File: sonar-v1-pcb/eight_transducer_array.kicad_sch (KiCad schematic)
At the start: 22 parts, among them U201 ADS8568SPM

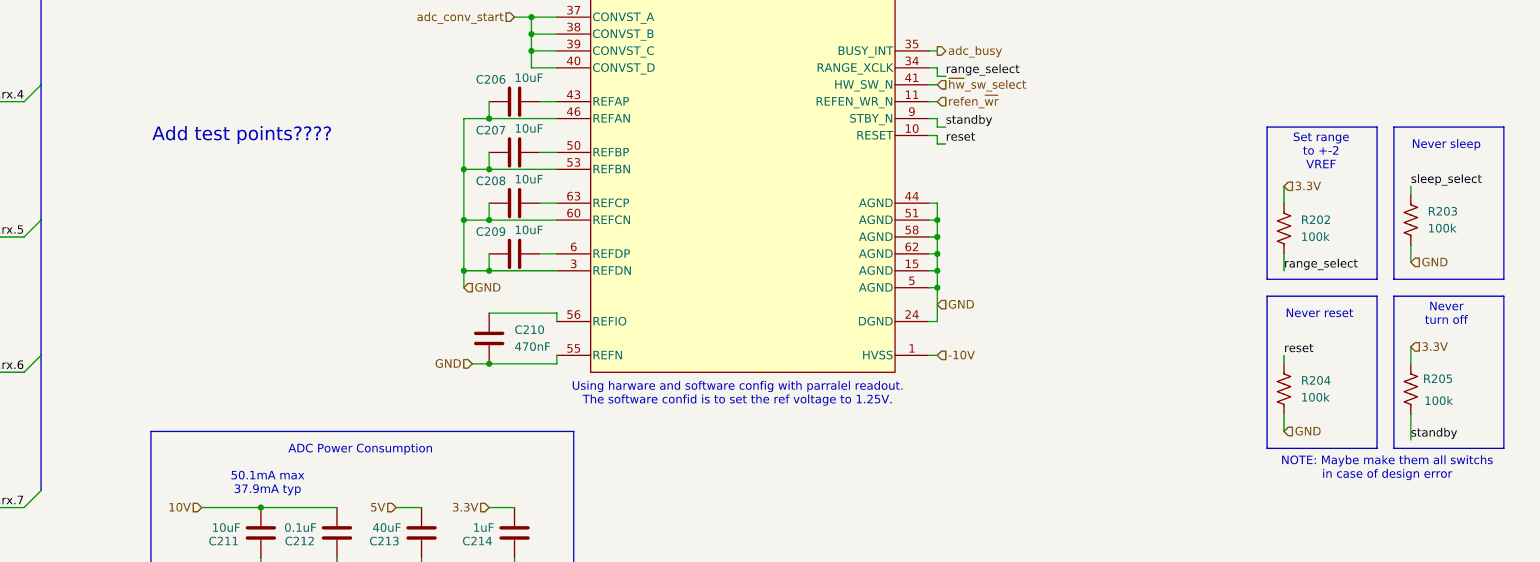
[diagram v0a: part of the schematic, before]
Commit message: Update inverting buck boost schematic
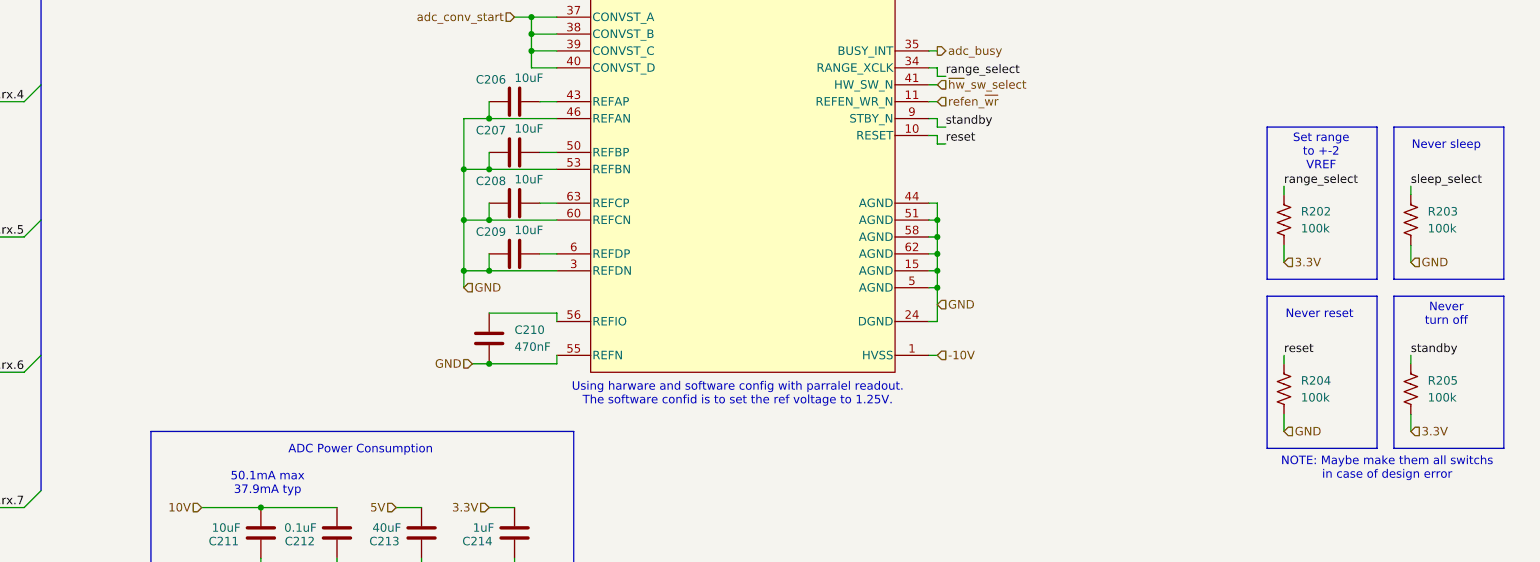
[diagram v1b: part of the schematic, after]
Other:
- note removed: "Add test points????"
- moved on the sheet: R202, R205
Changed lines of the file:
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@@
 		)
 	)
-	(text "Add test points????"
-		(exclude_from_sim no)
-		(at 91.186 113.03 0)
-		(effects
-			(font
-				(size 2.032 2.032)
-			)
-		)
-	)
 	(text "208mA max draw on \n+2.5V and -2.5V rails"
 		(exclude_from_sim no)
@@
 	(wire
 		(pts
-			(xy 266.7 147.32) (xy 266.7 144.78)
+			(xy 266.7 154.94) (xy 266.7 157.48)
 		)
 		(stroke
@@
 	(wire
 		(pts
+			(xy 247.65 129.54) (xy 247.65 132.08)
+		)
+		(stroke
+			(width 0)
+			(type default)
+		)
+	)
+	(wire
+		(pts
 			(xy 135.89 34.29) (xy 138.43 34.29)
 		)
@@
 	(wire
 		(pts
-			(xy 247.65 120.65) (xy 247.65 123.19)
-		)
-		(stroke
-			(width 0)
-			(type default)
-		)
-	)
-	(wire
-		(pts
 			(xy 124.46 118.11) (xy 128.27 118.11)
 		)
@@
 	(wire
 		(pts
-			(xy 247.65 133.35) (xy 247.65 130.81)
+			(xy 194.31 62.23) (xy 222.25 62.23)
 		)
 		(stroke
@@
 	(wire
 		(pts
-			(xy 194.31 62.23) (xy 222.25 62.23)
+			(xy 247.65 120.65) (xy 247.65 121.92)
 		)
 		(stroke
@@
 	(wire
 		(pts
-			(xy 266.7 158.75) (xy 266.7 154.94)
+			(xy 266.7 146.05) (xy 266.7 147.32)
 		)
 		(stroke
@@
 	)
 	(label "standby"
-		(at 266.7 158.75 0)
+		(at 266.7 146.05 0)
 		(effects
 			(font
@@
 	)
 	(label "range_select"
-		(at 247.65 133.35 0)
+		(at 247.65 120.65 0)
 		(effects
 			(font
@@
 	(hierarchical_label "3.3V"
 		(shape input)
-		(at 266.7 144.78 0)
+		(at 266.7 157.48 0)
 		(effects
 			(font
@@
 	(hierarchical_label "3.3V"
 		(shape input)
-		(at 247.65 120.65 0)
+		(at 247.65 132.08 0)
 		(effects
 			(font
@@
 	(symbol
 		(lib_id "Device:R_US")
-		(at 266.7 151.13 180)
+		(at 266.7 151.13 0)
 		(unit 1)
 		(exclude_from_sim no)
@@
 		(on_board yes)
 		(dnp no)
+		(fields_autoplaced yes)
 		(property "Reference" "R205"
-			(at 273.05 149.606 0)
+			(at 269.24 149.8599 0)
 			(effects
 				(font
@@
 		)
 		(property "Value" "100k"
-			(at 273.05 152.908 0)
+			(at 269.24 152.3999 0)
 			(effects
 				(font
@@
 		)
 		(property "Footprint" "Resistor_SMD:R_0402_1005Metric"
-			(at 265.684 150.876 90)
+			(at 267.716 151.384 90)
 			(effects
 				(font
@@
 	(symbol
 		(lib_id "Device:R_US")
-		(at 247.65 127 180)
+		(at 247.65 125.73 0)
 		(unit 1)
 		(exclude_from_sim no)
@@
 		(fields_autoplaced yes)
 		(property "Reference" "R202"
-			(at 250.19 125.7299 0)
+			(at 250.19 124.4599 0)
 			(effects
 				(font
 					(size 1.27 1.27)
 				)
-				(justify right)
+				(justify left)
 			)
 		)
 		(property "Value" "100k"
-			(at 250.19 128.2699 0)
+			(at 250.19 126.9999 0)
 			(effects
 				(font
 					(size 1.27 1.27)
 				)
-				(justify right)
+				(justify left)
 			)
 		)
 		(property "Footprint" "Resistor_SMD:R_0402_1005Metric"
-			(at 246.634 126.746 90)
+			(at 248.666 125.984 90)
 			(effects
 				(font
@@
 		)
 		(property "Datasheet" "~"
-			(at 247.65 127 0)
+			(at 247.65 125.73 0)
 			(effects
 				(font
@@
 		)
 		(property "Description" "Resistor, US symbol"
-			(at 247.65 127 0)
+			(at 247.65 125.73 0)
 			(effects
 				(font
@@
 		)
 		(fill
-			(color 194 194 194 1.0000)
+			(color 0 0 0 0.0000)
 		)
 		(property "Sheetname" "rx_amp_7"
@@
 		)
 		(fill
-			(color 194 194 194 1.0000)
+			(color 0 0 0 0.0000)
 		)
 		(property "Sheetname" "rx_amp_2"
@@
 		)
 		(fill
-			(color 194 194 194 1.0000)
+			(color 0 0 0 0.0000)
 		)
 		(property "Sheetname" "rx_amp_1"
@@
 		)
 		(fill
-			(color 194 194 194 1.0000)
+			(color 0 0 0 0.0000)
 		)
 		(property "Sheetname" "rx_amp_5"
@@
 		)
 		(fill
-			(color 194 194 194 1.0000)
+			(color 0 0 0 0.0000)
 		)
 		(property "Sheetname" "rx_amp_0"
@@
 		)
 		(fill
-			(color 194 194 194 1.0000)
+			(color 0 0 0 0.0000)
 		)
 		(property "Sheetname" "rx_amp_4"
@@
 		)
 		(fill
-			(color 194 194 194 1.0000)
+			(color 0 0 0 0.0000)
 		)
 		(property "Sheetname" "rx_amp_3"
@@
 		)
 		(fill
-			(color 194 194 194 1.0000)
+			(color 0 0 0 0.0000)
 		)
 		(property "Sheetname" "rx_amp_6"

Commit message: formatting lol
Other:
- note added: "Add test points????"
- moved on the sheet: R202, R205
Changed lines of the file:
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@@
 		)
 	)
+	(text "Add test points????"
+		(exclude_from_sim no)
+		(at 91.186 113.03 0)
+		(effects
+			(font
+				(size 2.032 2.032)
+			)
+		)
+	)
 	(text "208mA max draw on \n+2.5V and -2.5V rails"
 		(exclude_from_sim no)
@@
 	(wire
 		(pts
-			(xy 266.7 154.94) (xy 266.7 157.48)
+			(xy 266.7 147.32) (xy 266.7 144.78)
 		)
 		(stroke
@@
 	(wire
 		(pts
-			(xy 247.65 129.54) (xy 247.65 132.08)
-		)
-		(stroke
-			(width 0)
-			(type default)
-		)
-	)
-	(wire
-		(pts
 			(xy 135.89 34.29) (xy 138.43 34.29)
 		)
@@
 	(wire
 		(pts
+			(xy 247.65 120.65) (xy 247.65 123.19)
+		)
+		(stroke
+			(width 0)
+			(type default)
+		)
+	)
+	(wire
+		(pts
 			(xy 124.46 118.11) (xy 128.27 118.11)
 		)
@@
 	(wire
 		(pts
-			(xy 194.31 62.23) (xy 222.25 62.23)
+			(xy 247.65 133.35) (xy 247.65 130.81)
 		)
 		(stroke
@@
 	(wire
 		(pts
-			(xy 247.65 120.65) (xy 247.65 121.92)
+			(xy 194.31 62.23) (xy 222.25 62.23)
 		)
 		(stroke
@@
 	(wire
 		(pts
-			(xy 266.7 146.05) (xy 266.7 147.32)
+			(xy 266.7 158.75) (xy 266.7 154.94)
 		)
 		(stroke
@@
 	)
 	(label "standby"
-		(at 266.7 146.05 0)
+		(at 266.7 158.75 0)
 		(effects
 			(font
@@
 	)
 	(label "range_select"
-		(at 247.65 120.65 0)
+		(at 247.65 133.35 0)
 		(effects
 			(font
@@
 	(hierarchical_label "3.3V"
 		(shape input)
-		(at 266.7 157.48 0)
+		(at 266.7 144.78 0)
 		(effects
 			(font
@@
 	(hierarchical_label "3.3V"
 		(shape input)
-		(at 247.65 132.08 0)
+		(at 247.65 120.65 0)
 		(effects
 			(font
@@
 	(symbol
 		(lib_id "Device:R_US")
-		(at 266.7 151.13 0)
+		(at 266.7 151.13 180)
 		(unit 1)
 		(exclude_from_sim no)
@@
 		(on_board yes)
 		(dnp no)
-		(fields_autoplaced yes)
 		(property "Reference" "R205"
-			(at 269.24 149.8599 0)
+			(at 273.05 149.606 0)
 			(effects
 				(font
@@
 		)
 		(property "Value" "100k"
-			(at 269.24 152.3999 0)
+			(at 273.05 152.908 0)
 			(effects
 				(font
@@
 		)
 		(property "Footprint" "Resistor_SMD:R_0402_1005Metric"
-			(at 267.716 151.384 90)
+			(at 265.684 150.876 90)
 			(effects
 				(font
@@
 	(symbol
 		(lib_id "Device:R_US")
-		(at 247.65 125.73 0)
+		(at 247.65 127 180)
 		(unit 1)
 		(exclude_from_sim no)
@@
 		(fields_autoplaced yes)
 		(property "Reference" "R202"
-			(at 250.19 124.4599 0)
+			(at 250.19 125.7299 0)
 			(effects
 				(font
 					(size 1.27 1.27)
 				)
-				(justify left)
+				(justify right)
 			)
 		)
 		(property "Value" "100k"
-			(at 250.19 126.9999 0)
+			(at 250.19 128.2699 0)
 			(effects
 				(font
 					(size 1.27 1.27)
 				)
-				(justify left)
+				(justify right)
 			)
 		)
 		(property "Footprint" "Resistor_SMD:R_0402_1005Metric"
-			(at 248.666 125.984 90)
+			(at 246.634 126.746 90)
 			(effects
 				(font
@@
 		)
 		(property "Datasheet" "~"
-			(at 247.65 125.73 0)
+			(at 247.65 127 0)
 			(effects
 				(font
@@
 		)
 		(property "Description" "Resistor, US symbol"
-			(at 247.65 125.73 0)
+			(at 247.65 127 0)
 			(effects
 				(font
@@
 		)
 		(fill
-			(color 0 0 0 0.0000)
+			(color 194 194 194 1.0000)
 		)
 		(property "Sheetname" "rx_amp_7"
@@
 		)
 		(fill
-			(color 0 0 0 0.0000)
+			(color 194 194 194 1.0000)
 		)
 		(property "Sheetname" "rx_amp_2"
@@
 		)
 		(fill
-			(color 0 0 0 0.0000)
+			(color 194 194 194 1.0000)
 		)
 		(property "Sheetname" "rx_amp_1"
@@
 		)
 		(fill
-			(color 0 0 0 0.0000)
+			(color 194 194 194 1.0000)
 		)
 		(property "Sheetname" "rx_amp_5"
@@
 		)
 		(fill
-			(color 0 0 0 0.0000)
+			(color 194 194 194 1.0000)
 		)
 		(property "Sheetname" "rx_amp_0"
@@
 		)
 		(fill
-			(color 0 0 0 0.0000)
+			(color 194 194 194 1.0000)
 		)
 		(property "Sheetname" "rx_amp_4"
@@
 		)
 		(fill
-			(color 0 0 0 0.0000)
+			(color 194 194 194 1.0000)
 		)
 		(property "Sheetname" "rx_amp_3"
@@
 		)
 		(fill
-			(color 0 0 0 0.0000)
+			(color 194 194 194 1.0000)
 		)
 		(property "Sheetname" "rx_amp_6"
